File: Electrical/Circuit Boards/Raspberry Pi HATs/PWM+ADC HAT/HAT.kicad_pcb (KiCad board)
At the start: 2 copper layers, 65 x 56 mm, 25 parts, among them J1 CONN_01X02, J10 CONN_01X03, J11 CONN_01X03, J12 CONN_01X03, J13 CONN_01X03, J14 CONN_01X03, J15 CONN_01X03, J16 CONN_01X03, J17 CONN_01X03, J18 CONN_01X03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

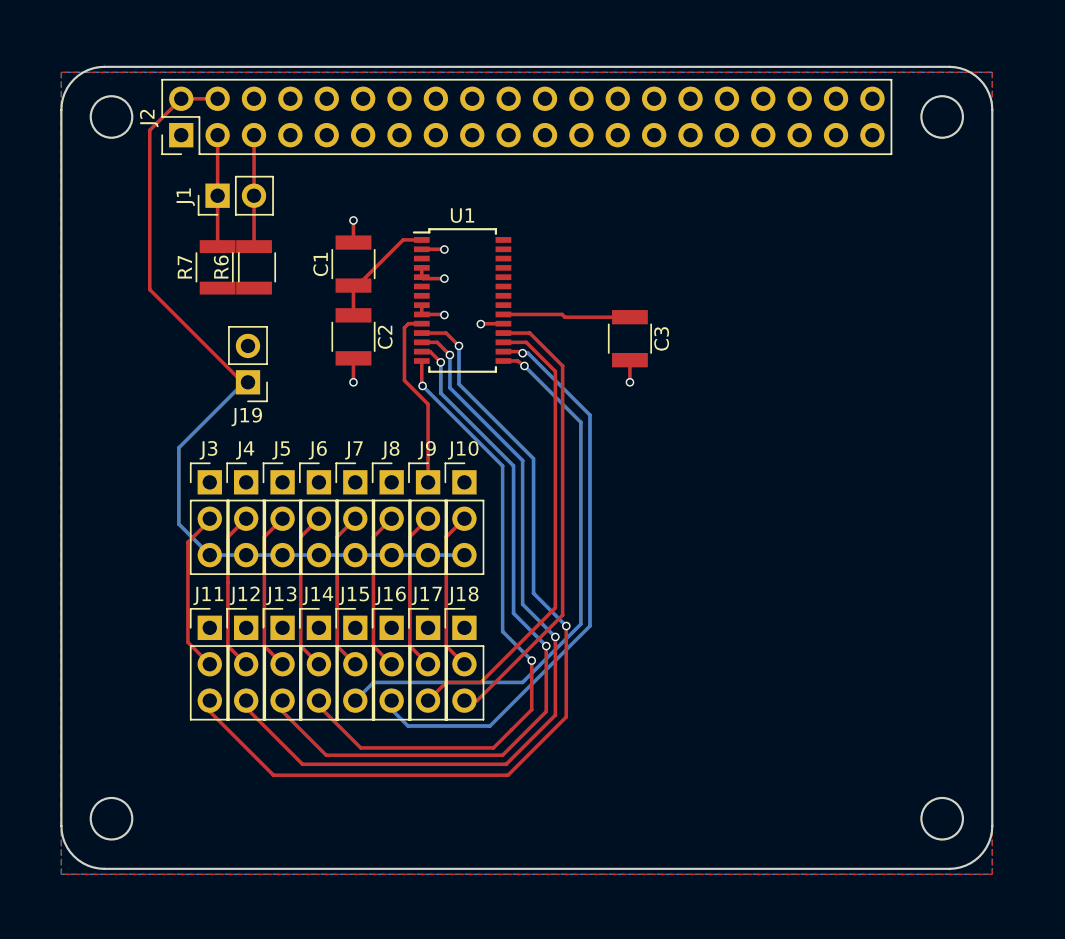
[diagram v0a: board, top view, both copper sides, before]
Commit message: Re-routed the ADC board (package type mistake)
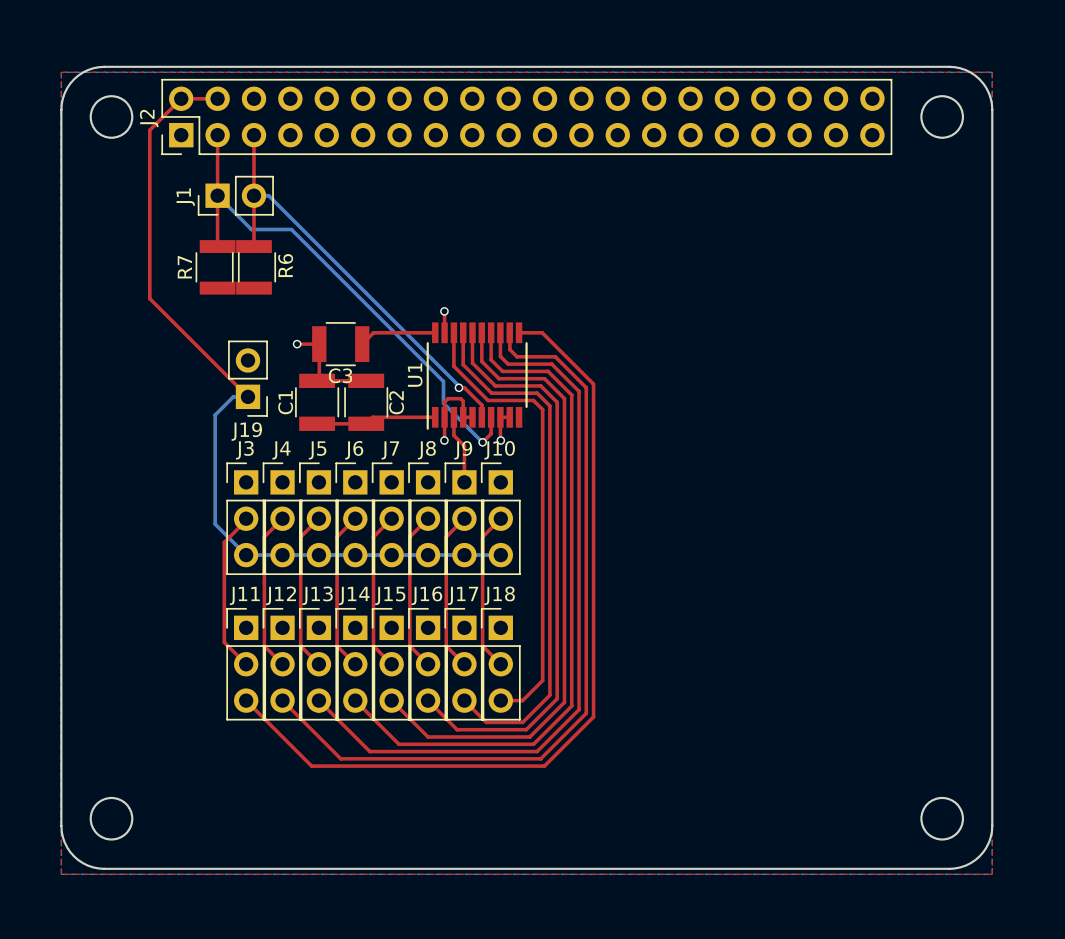
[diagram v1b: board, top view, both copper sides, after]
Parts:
- U1: footprint Housings_SSOP:TSSOP-28_4.4x9.7mm_Pitch0.65mm -> Housings_SSOP:TSSOP-20_4.4x6.5mm_Pitch0.65mm
- moved C3 20.2 mm to (119.5, 94.4), turned to 180 degrees
- moved C1 9.69 mm to (121.3, 98.4)
- moved U1 5.31 mm to (129.0, 96.5), turned to 90 degrees
- moved C2 5.23 mm to (117.9, 98.4), turned to 90 degrees
- moved J11 2.54 mm to (112.9, 114.2)
- moved J13 2.54 mm to (118.0, 114.2)
- moved J15 2.54 mm to (123.1, 114.2)
- moved J17 2.54 mm to (128.1, 114.2)
- moved J3 2.54 mm to (112.9, 104.0)
- moved J5 2.54 mm to (118.0, 104.0)
- moved J7 2.54 mm to (123.1, 104.0)
- moved J9 2.54 mm to (128.1, 104.0)
- moved J10 2.54 mm to (130.7, 104.0)
- moved J12 2.54 mm to (115.4, 114.2)
- moved J14 2.54 mm to (120.5, 114.2)
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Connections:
- U1 pad 6: (no net) -> /SCL
- U1 pad 7: (no net) -> /SDA
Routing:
- net /SDA: track 7.88 -> 36.4 mm, vias 0 -> 1
- net /SCL: track 7.88 -> 30.8 mm, vias 0 -> 1
- net +3V3: track 12.8 -> 4.85 mm
- net /A4: track 39.2 -> 44.2 mm, vias 1 -> 0
- net GND: track 12.5 -> 17.3 mm, vias 7 -> 4
- net /A6: track 32.5 -> 37.1 mm
- net /A0: track 61.2 -> 57.5 mm, vias 2 -> 0
- net Net-(C3-Pad1): track 8.91 -> 5.43 mm
- net /A3: track 45.1 -> 48.1 mm, vias 2 -> 0
- net /A2: track 50.8 -> 52.0 mm, vias 2 -> 0
- net /A5: track 40.5 -> 41.3 mm, vias 1 -> 0
- net /A1: track 55.7 -> 55.4 mm, vias 2 -> 0

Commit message: Add selectable ADC reference to ADC HAT
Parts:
- added J20: CONN_01X04_MALE, Pin_Headers:Pin_Header_Straight_1x04_Pitch2.54mm, F.Cu at (152.4, 90.2)
- added J21: CONN_01X03_MALE, Pin_Headers:Pin_Header_Straight_1x03_Pitch2.54mm, F.Cu at (149.9, 90.2)
- added R1: 0, Resistors_SMD:R_0603, F.Cu at (129.3, 94.2)
- added R2: 0, Resistors_SMD:R_0603, F.Cu at (129.3, 91.7)
- added R3: 0, Resistors_SMD:R_0603, F.Cu at (126.5, 94.2)
- added R4: 0, Resistors_SMD:R_0603, F.Cu at (126.5, 91.7)
- moved C3 26.2 mm to (144.8, 101.3), turned to 270 degrees
- moved U1 7.88 mm to (136.4, 93.7), turned to 0 degrees
- moved C1 1.55 mm to (121.5, 96.9), turned to 270 degrees
- moved C2 1.55 mm to (118.1, 96.9), turned to 270 degrees
- moved R6 0.25 mm to (113.7, 89.0)
- moved R7 0.25 mm to (110.7, 89.0)
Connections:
- C1 pad 2: GND -> Net-(C1-Pad2)
- C2 pad 2: GND -> Net-(C1-Pad2)
- U1 pad 10: +3V3 -> +5V
- U1 pad 20: Net-(C3-Pad1) -> Net-(J21-Pad2)
- U1 pad 3: +3V3 -> +5V
- U1 pad 4: GND -> Net-(R2-Pad2)
- U1 pad 5: GND -> Net-(R1-Pad2)
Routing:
- net +3V3: track 4.85 -> 52.0 mm, vias 0 -> 1
- net Net-(C1-Pad1): track 8.44 -> 50.2 mm, vias 0 -> 2
- net Net-(J21-Pad2): track 0.00 -> 11.5 mm
- net +5V: track 58.9 -> 68.8 mm, vias 0 -> 5
- net Net-(R2-Pad2): track 0.00 -> 7.08 mm
- net Net-(R1-Pad2): track 0.00 -> 6.99 mm
- net /A1: track 55.4 -> 50.5 mm
- net /A0: track 57.5 -> 52.7 mm
- net GND: track 17.3 -> 13.3 mm, vias 4 -> 5
- net /A2: track 52.0 -> 48.1 mm
- net Net-(C1-Pad2): track 0.00 -> 3.43 mm
- net /A3: track 48.1 -> 45.0 mm
- net /SCL: track 30.8 -> 33.9 mm, vias 1 -> 0
- net Net-(C3-Pad1): track 5.43 -> 8.47 mm
- net Net-(J20-Pad3): track 0.00 -> 2.54 mm
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- added copper zone on F.Cu, net +5V
- removed copper zone on F.Cu, net +3V3
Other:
- board text added: "0"
- board text added: "1"
- board text added: "3v3"
- board text added: "5V"
- board text added: "AD0"
- board text added: "AD1"
- board text added: "CH0"
- board text added: "CH1"
- board text added: "CH2"
- board text added: "CH3"
- board text added: "CH4"
- board text added: "CH5"
- board text added: "CH6"
- board text added: "CH7"
- board text added: "Float"
- board text added: "Gnd"
- board text added: "Only attach when VREF is grounded"
- board text added: "Other"
- board text added: "REFCOMP"
- board text added: "Sig"
- board text added: "V+"
- board text added: "VREF"
